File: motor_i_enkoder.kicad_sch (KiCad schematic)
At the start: 14 parts, among them J5 Conn_01x02, J6 Conn_02x05, M2 Motor_DC, SW3 RotaryEncoder, U5 L298N

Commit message: Add files via upload
Jeszcze PCB
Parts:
- removed J5: Conn_01x02, symbol Connector_Generic:Conn_01x02
- removed J6: Conn_02x05, symbol Connector_Generic:Conn_02x05_Counter_Clockwise
- added J7: Conn_02x06_Odd_Even, symbol Connector_Generic:Conn_02x06_Odd_Even
- C11: renamed from 100u/16V2; value C6 -> 100uF/16V
- C12: renamed from 100n1; value C5 -> 100nF
- R10: renamed from 1k2; value R -> 1k
- R9: renamed from 1k1; value R -> 1k
- renumbered D6 to D4, D10 to D5, D7 to D6, D11 to D7, M2 to M1, SW3 to SW2, U5 to U4
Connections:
- net CPU_GND: now also J7.9 (Pin_9)
- net DRIVER IN1: now also J7.2 (Pin_2)
- net DRIVER IN2: now also J7.4 (Pin_4)
- net DRIVER IN3: now also J7.8 (Pin_8)
- net DRIVER IN4: now also J7.10 (Pin_10)
- net ENC A: now also J7.11 (Pin_11)
- net ENC B: now also J7.12 (Pin_12)
- net GND: now also J7.7 (Pin_7)
- net PWM A: now also J7.6 (Pin_6)
- net 5V Z LM renamed Vcc
- net Vcc: now also J7.3 (Pin_3)
- net VDD renamed Vdd
- net Vdd: now also J7.5 (Pin_5)
- net ZASILANIE 12V renamed 12V
- net 12V: now also J7.1 (Pin_1)

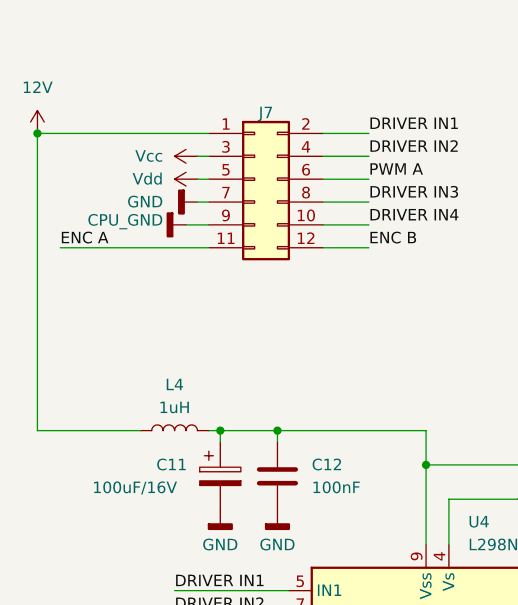
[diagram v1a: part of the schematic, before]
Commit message: poprawki po 'pracy' michala na schemacie. Poprawione PCB pamieci po Kubie. Grubsze sciezki, poprawiona pozycja decoupling capacitora
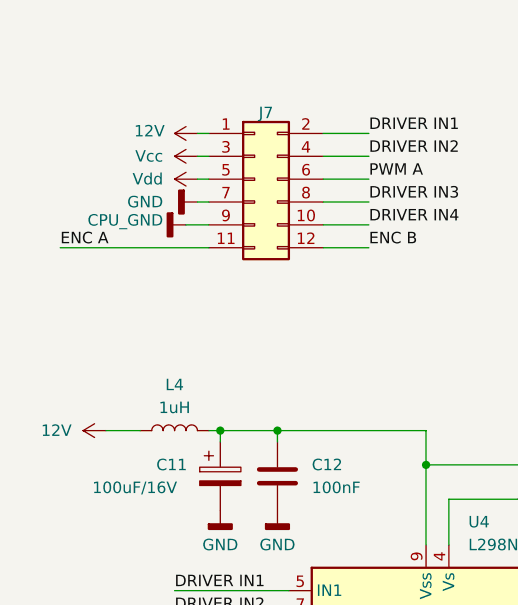
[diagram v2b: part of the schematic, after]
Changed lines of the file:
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@@
-	)
-	(junction
-		(at 19.05 30.48)
-		(diameter 0)
-		(color 0 0 0 0)
 	)
 	(junction
@@
 	(wire
 		(pts
-			(xy 19.05 30.48) (xy 38.1 30.48)
+			(xy 36.83 30.48) (xy 38.1 30.48)
 		)
 		(stroke
@@
 	(wire
 		(pts
-			(xy 30.48 63.5) (xy 19.05 63.5)
+			(xy 30.48 63.5) (xy 26.67 63.5)
 		)
 		(stroke
@@
 		(pts
 			(xy 62.23 67.31) (xy 87.63 67.31)
-		)
-		(stroke
-			(width 0)
-			(type default)
-		)
-	)
-	(wire
-		(pts
-			(xy 19.05 30.48) (xy 19.05 63.5)
 		)
 		(stroke
@@
 	)
 	(symbol
+		(lib_id "power:+1V0")
+		(at 26.67 63.5 90)
+		(unit 1)
+		(body_style 1)
+		(exclude_from_sim no)
+		(in_bom yes)
+		(on_board yes)
+		(in_pos_files yes)
+		(dnp no)
+		(fields_autoplaced yes)
+		(property "Reference" "#PWR054"
+			(at 30.48 63.5 0)
+			(hide yes)
+			(show_name no)
+			(do_not_autoplace no)
+			(effects
+				(font
+					(size 1.27 1.27)
+				)
+			)
+		)
+		(property "Value" "12V"
+			(at 22.86 63.4999 90)
+			(show_name no)
+			(do_not_autoplace no)
+			(effects
+				(font
+					(size 1.27 1.27)
+				)
+				(justify left)
+			)
+		)
+		(property "Footprint" ""
+			(at 26.67 63.5 0)
+			(hide yes)
+			(show_name no)
+			(do_not_autoplace no)
+			(effects
+				(font
+					(size 1.27 1.27)
+				)
+			)
+		)
+		(property "Datasheet" ""
+			(at 26.67 63.5 0)
+			(hide yes)
+			(show_name no)
+			(do_not_autoplace no)
+			(effects
+				(font
+					(size 1.27 1.27)
+				)
+			)
+		)
+		(property "Description" "Power symbol creates a global label with name \"+1V0\""
+			(at 26.67 63.5 0)
+			(hide yes)
+			(show_name no)
+			(do_not_autoplace no)
+			(effects
+				(font
+					(size 1.27 1.27)
+				)
+			)
+		)
+		(pin "1"
+		)
+		(instances
+			(project "smiw_proj"
+				(path "/1f242d25-3f72-47fa-ab49-33cac50f3366"
+					(reference "#PWR054")
+					(unit 1)
+				)
+			)
+		)
+	)
+	(symbol
 		(lib_id "Device:L")
 		(at 34.29 63.5 90)
@@
 	(symbol
 		(lib_id "power:+1V0")
-		(at 19.05 30.48 0)
+		(at 36.83 30.48 90)
 		(unit 1)
 		(body_style 1)
@@
 		(in_pos_files yes)
 		(dnp no)
-		(fields_autoplaced yes)
 		(property "Reference" "#PWR043"
-			(at 19.05 34.29 0)
+			(at 40.64 30.48 0)
 			(hide yes)
 			(show_name no)
@@
 		)
 		(property "Value" "12V"
-			(at 19.05 25.4 0)
+			(at 31.496 30.226 90)
 			(show_name no)
 			(do_not_autoplace no)
@@
 		)
 		(property "Footprint" ""
-			(at 19.05 30.48 0)
+			(at 36.83 30.48 0)
 			(hide yes)
 			(show_name no)
@@
 		)
 		(property "Datasheet" ""
-			(at 19.05 30.48 0)
+			(at 36.83 30.48 0)
 			(hide yes)
 			(show_name no)
@@
 		)
 		(property "Description" "Power symbol creates a global label with name \"+1V0\""
-			(at 19.05 30.48 0)
-			(hide yes)
-			(show_name no)
+			(at 36.83 30.48 0)
+			(hide yes)
+			(show_name no)

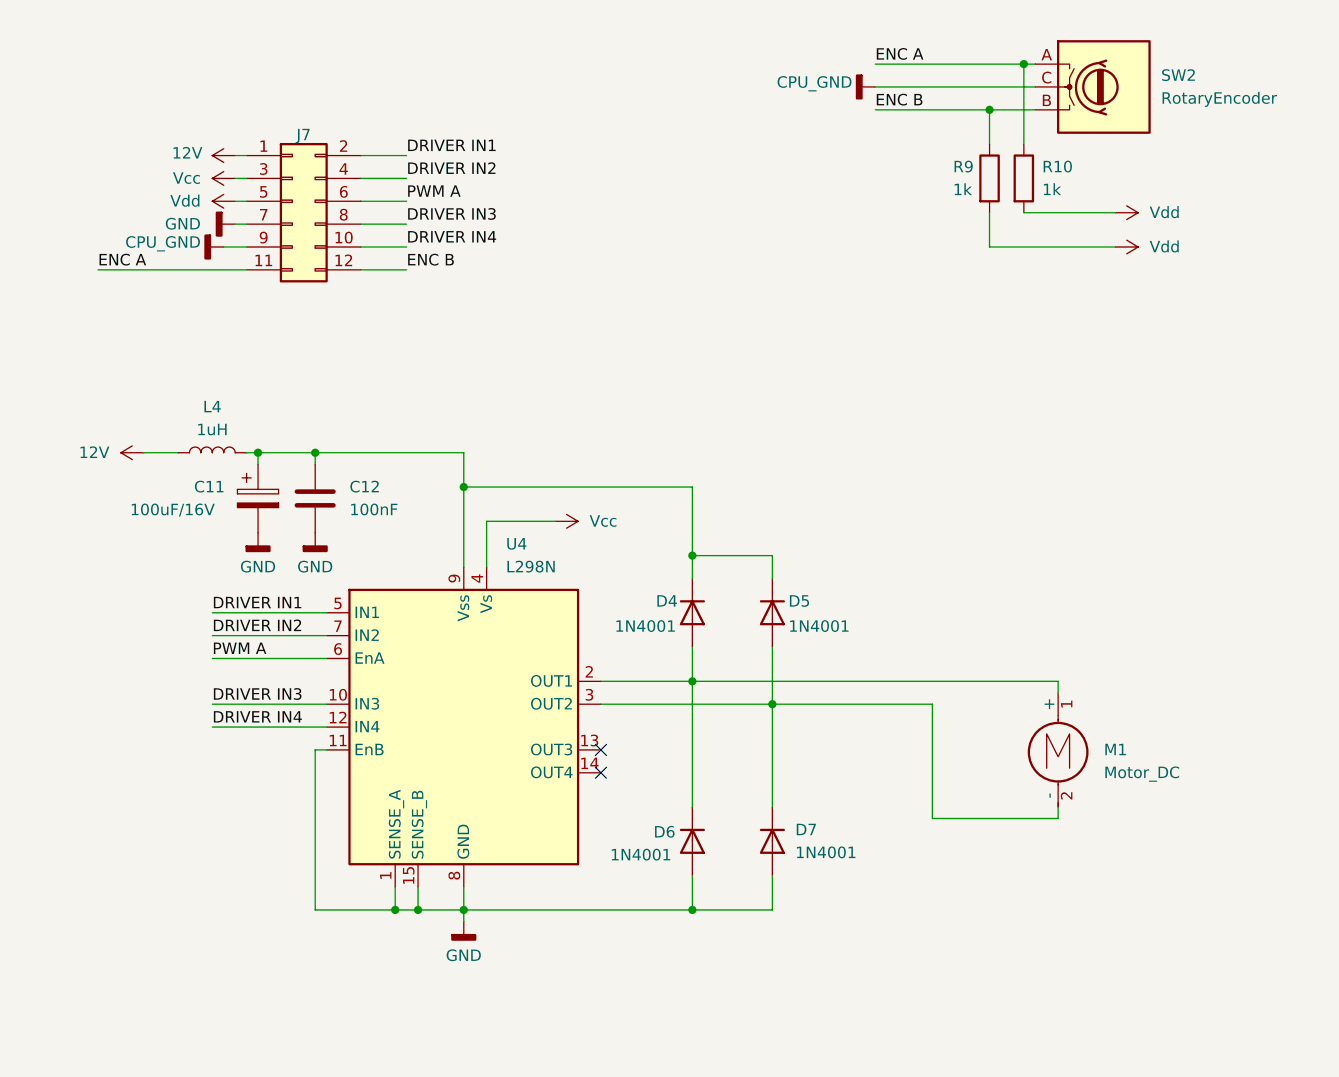
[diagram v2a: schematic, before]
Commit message: dodane footprinty
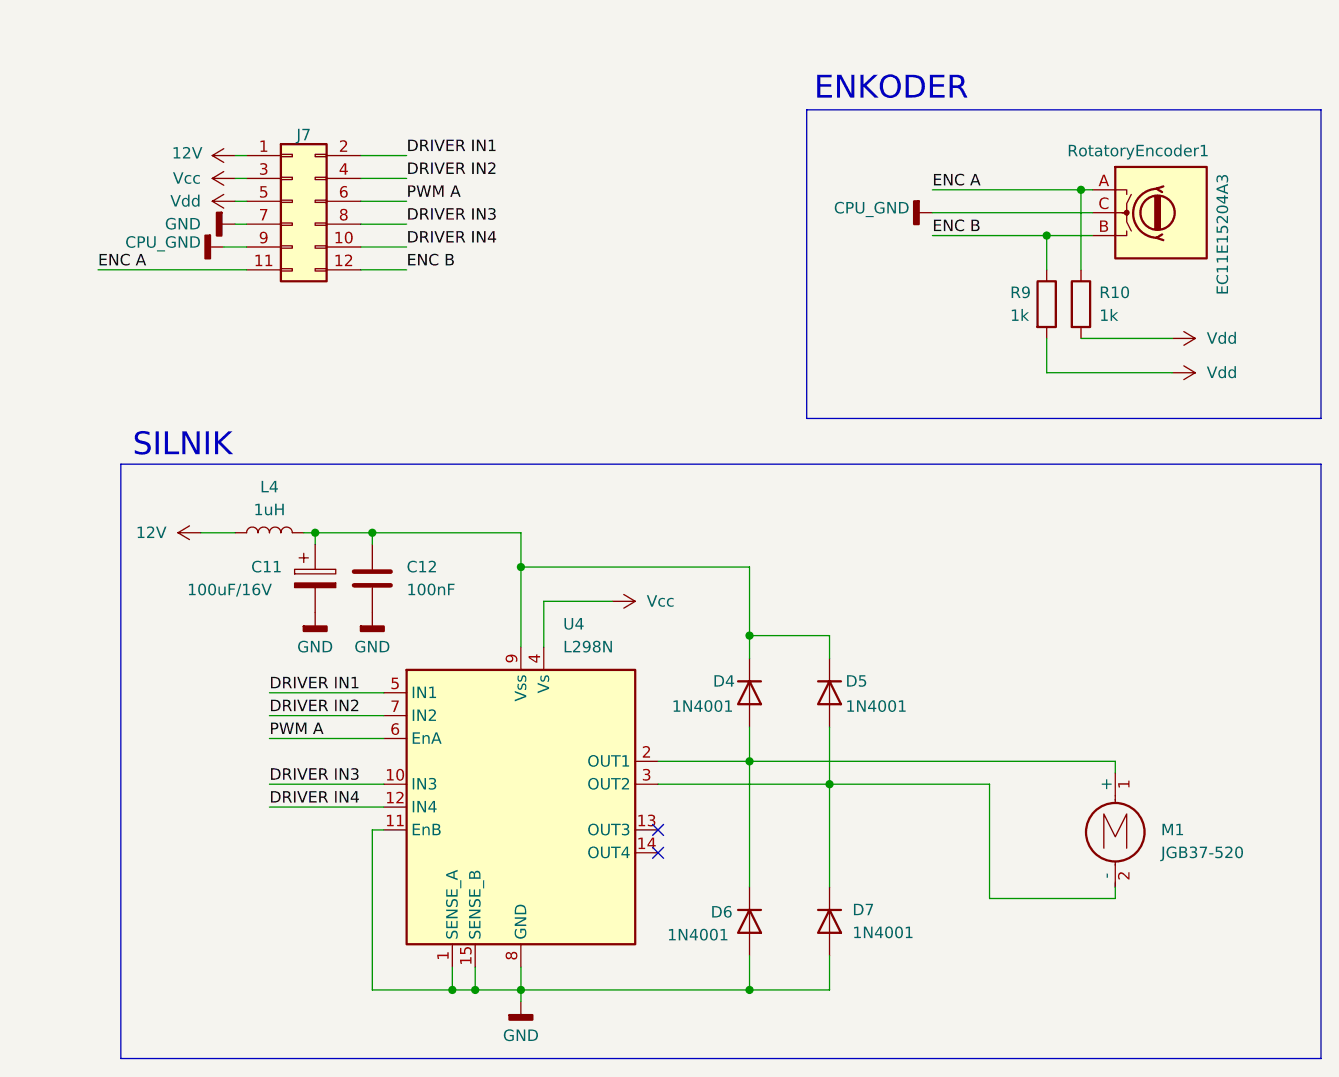
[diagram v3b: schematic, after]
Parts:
- C11: footprint (none) -> Capacitor_THT:CP_Axial_L10.0mm_D4.5mm_P15.00mm_Horizontal
- C12: footprint (none) -> Capacitor_SMD:C_0805_2012Metric
- D4, D5, D6, D7: footprint (none) -> Diode_THT:D_DO-41_SOD81_P10.16mm_Horizontal
- J7: footprint (none) -> Connector_PinHeader_2.54mm:PinHeader_2x06_P2.54mm_Vertical
- L4: footprint (none) -> Inductor_SMD:L_0805_2012Metric
- M1: value Motor_DC -> JGB37-520; footprint (none) -> TerminalBlock_MetzConnect:TerminalBlock_MetzConnect_Type011_RT05502HBLC_1x02_P5.00mm_Horizontal
- R10, R9: footprint (none) -> Resistor_SMD:R_0805_2012Metric
- RotatoryEncoder1: renamed from SW2; value RotaryEncoder -> EC11E15204A3; footprint (none) -> Rotary_Encoder:RotaryEncoder_Alps_EC11E_Vertical_H20mm
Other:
- note added: "ENKODER"
- note added: "SILNIK"
- moved on the sheet: C11, C12, D4, D5, D6, D7, L4, R10, R9, RotatoryEncoder1, U4
